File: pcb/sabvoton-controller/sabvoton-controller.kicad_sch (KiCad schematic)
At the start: 48 parts, among them J1 CONTROLLER_HALL, J2 CONN_MAIN, J3 ENGINE_HALL, J4 DISPLAY_CONNECTOR, Q1 BSS123, Q2 BSS123, Q3 BSS123, U1 ESP32-WROOM-32, U2 XL7015E1, U3 XL7015E1, U4 NCP1117-3.3_SOT223, U5 LM1117-1.8, U6 BTS4140N, U7 LM358

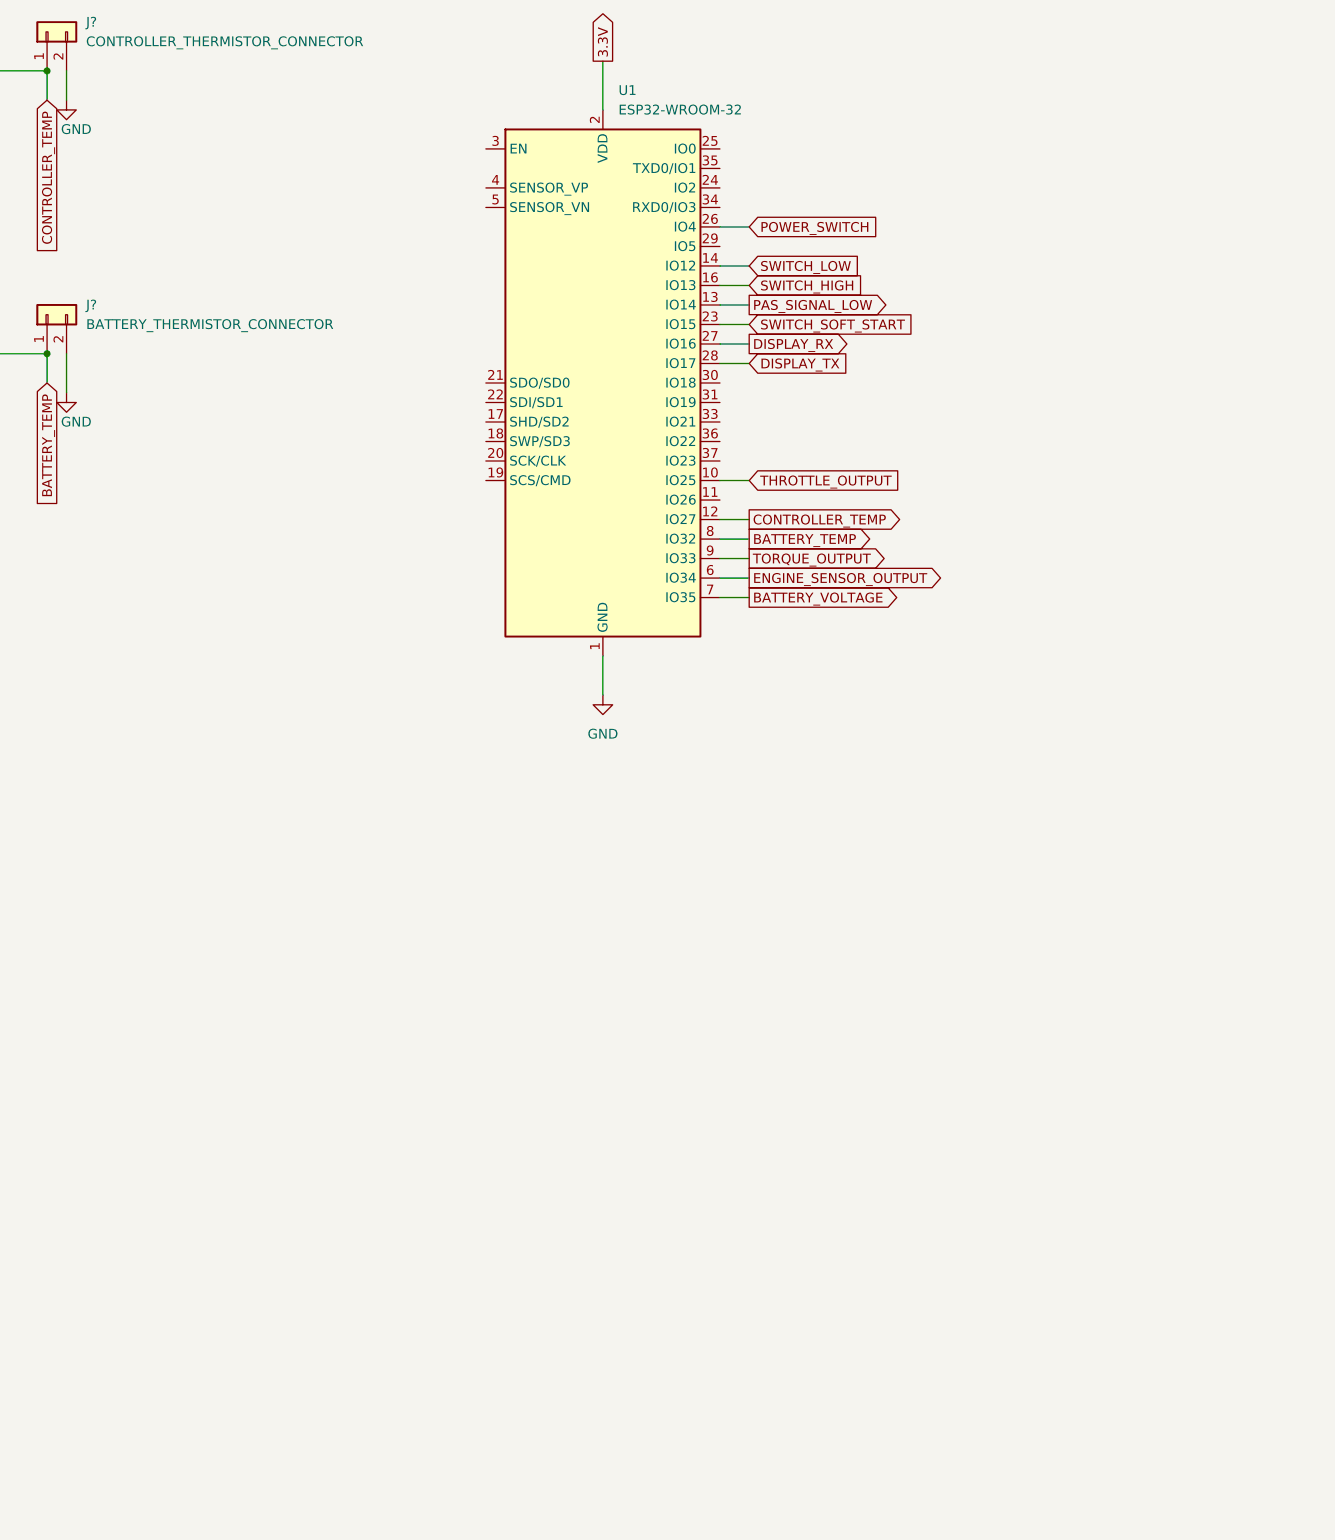
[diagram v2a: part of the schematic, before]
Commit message: Added USB connector
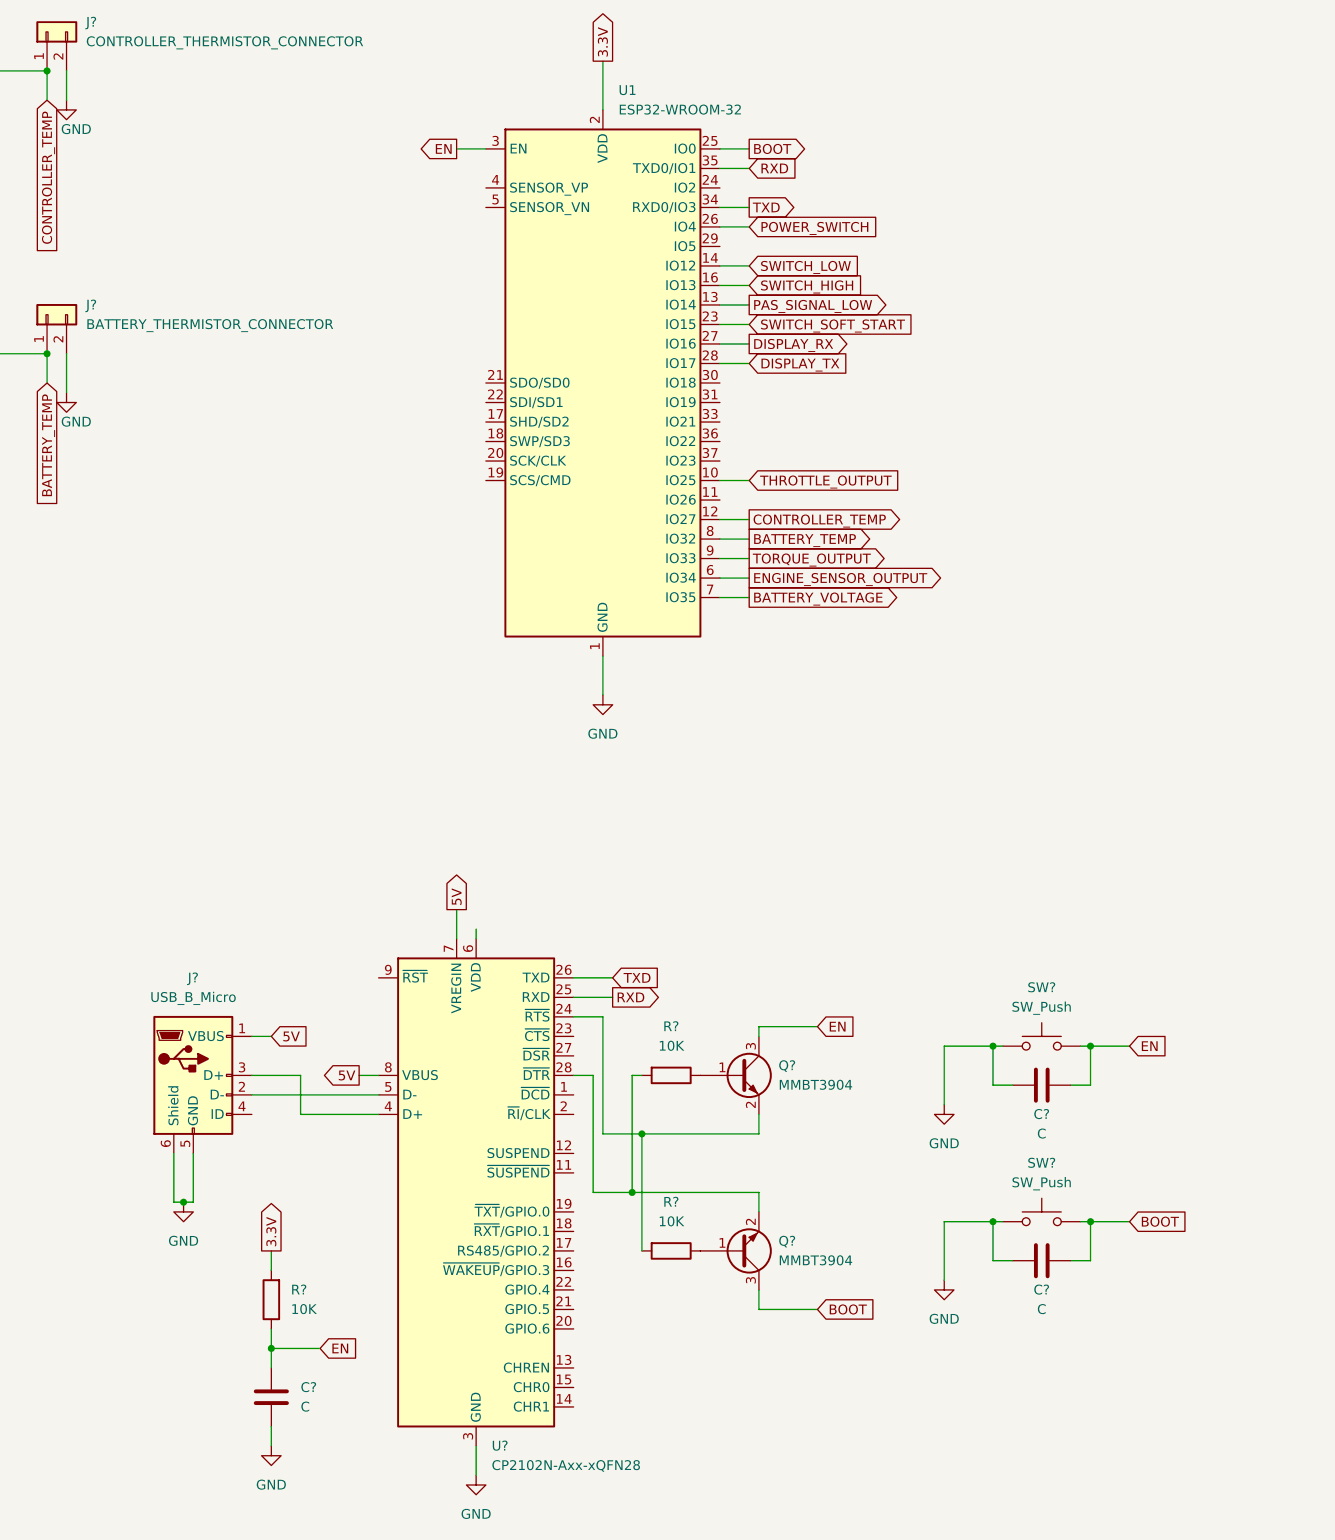
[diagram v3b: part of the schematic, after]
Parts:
- added C? (x3): C, symbol Device:C
- added J?: USB_B_Micro, symbol Connector:USB_B_Micro
- added Q? (x2): MMBT3904, Package_TO_SOT_SMD:SOT-23, symbol Transistor_BJT:MMBT3904
- added R? (x3): 10K, symbol Device:R
- added SW? (x2): SW_Push, symbol Switch:SW_Push
- added U?: CP2102N-Axx-xQFN28, Package_DFN_QFN:QFN-28-1EP_5x5mm_P0.5mm_EP3.35x3.35mm, symbol Interface_USB:CP2102N-Axx-xQFN28
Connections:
- net 3.3V: now also R?.2
- net 5V: now also J?.1 (VBUS), U?.7 (VREGIN), U?.8 (VBUS)
- net GND: now also C?.1, C?.1, C?.2, J?.5 (GND), J?.6 (Shield), SW?.1, SW?.1, U?.29 (GND), U?.3 (GND)
- net BOOT: now reaches U1.25 (IO0)
- net BOOT: now also C?.2, Q?.3 (C), SW?.2
- net EN: now reaches U1.3 (EN)
- net EN: now also C?.1, C?.2, Q?.3 (C), R?.1, SW?.2
- net TXD: now reaches U1.34 (RXD0/IO3)
- net TXD: now also U?.26 (TXD)
- net RXD: now reaches U1.35 (TXD0/IO1)
- net RXD: now also U?.25 (RXD)
- new net: Q?.1 (B), R?.1 (x2)
- new net: Q?.2 (E), R?.2, U?.24 (~{RTS})
- new net: J?.2 (D-), U?.5 (D-)
- new net: J?.3 (D+), U?.4 (D+)
- new net: Q?.2 (E), R?.2, U?.28 (~{DTR})

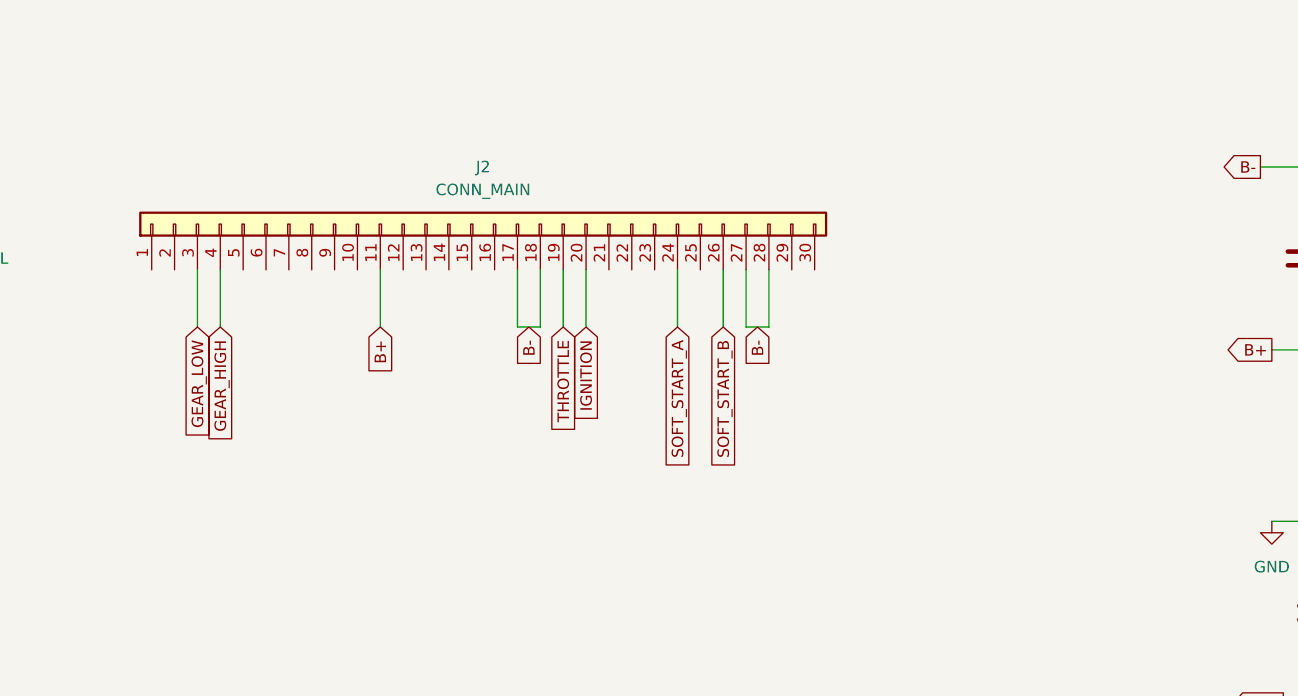
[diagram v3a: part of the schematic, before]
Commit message: Added programing connector
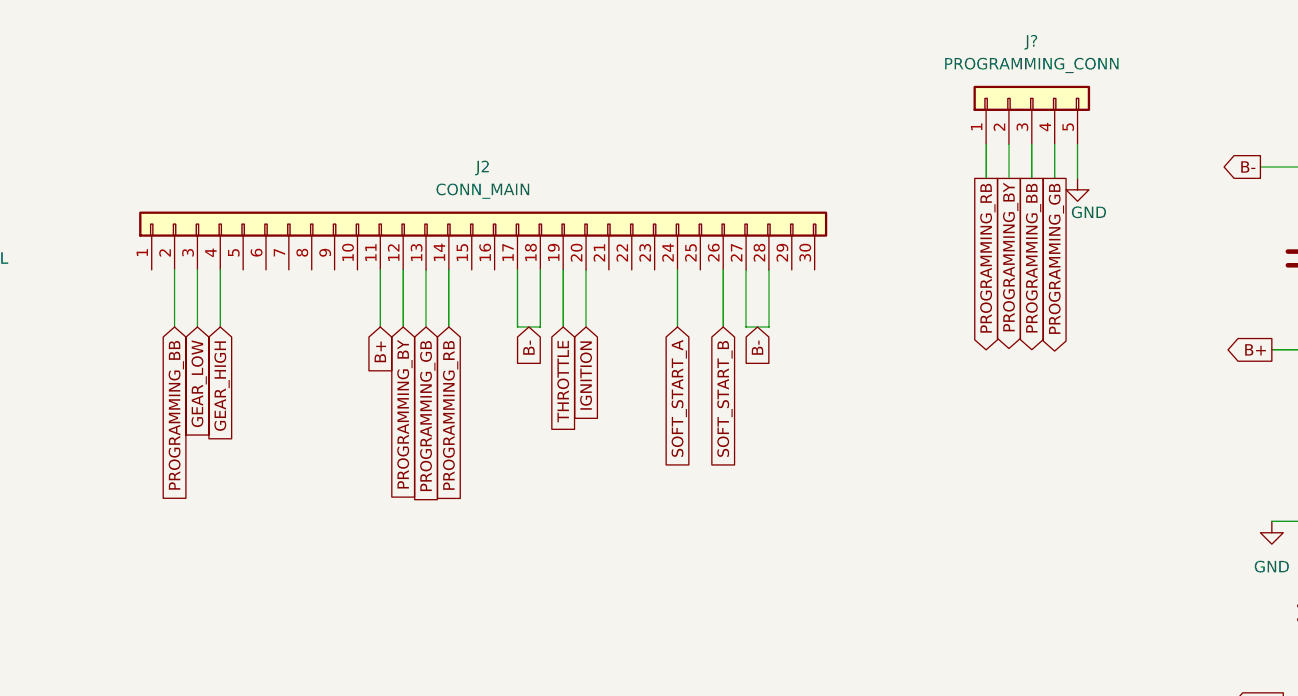
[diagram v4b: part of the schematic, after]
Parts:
- added J?: PROGRAMMING_CONN, symbol Connector_Generic:Conn_01x05
- J?: footprint (none) -> Connector_USB:USB_C_Plug_Molex_105444
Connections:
- net GND: now also J?.5 (Pin_5)
- net PROGRAMMING_BY: now reaches J2.12 (Pin_12)
- net PROGRAMMING_BY: now also J?.2 (Pin_2)
- net PROGRAMMING_GB: now reaches J2.13 (Pin_13)
- net PROGRAMMING_GB: now also J?.4 (Pin_4)
- net PROGRAMMING_RB: now reaches J2.14 (Pin_14)
- net PROGRAMMING_RB: now also J?.1 (Pin_1)
- net PROGRAMMING_BB: now reaches J2.2 (Pin_2)
- net PROGRAMMING_BB: now also J?.3 (Pin_3)
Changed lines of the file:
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@@
+    (stroke (width 0) (type default) (color 0 0 0 0))
+  )
+  (wire (pts (xy 472.44 45.72) (xy 472.44 49.53))
     (stroke (width 0) (type default) (color 0 0 0 0))
   )
@@
     (stroke (width 0) (type default) (color 0 0 0 0))
   )
+  (wire (pts (xy 467.36 45.72) (xy 467.36 49.53))
+    (stroke (width 0) (type default) (color 0 0 0 0))
+  )
   (wire (pts (xy 241.3 128.27) (xy 241.3 134.62))
     (stroke (width 0) (type default) (color 0 0 0 0))
   )
+  (wire (pts (xy 469.9 45.72) (xy 469.9 49.53))
+    (stroke (width 0) (type default) (color 0 0 0 0))
+  )
   (wire (pts (xy 519.43 147.32) (xy 521.97 147.32))
     (stroke (width 0) (type default) (color 0 0 0 0))
@@
     (stroke (width 0) (type default) (color 0 0 0 0))
   )
+  (wire (pts (xy 372.11 59.69) (xy 372.11 66.04))
+    (stroke (width 0) (type default) (color 0 0 0 0))
+  )
   (wire (pts (xy 398.78 267.97) (xy 398.78 265.43))
     (stroke (width 0) (type default) (color 0 0 0 0))
@@
     (stroke (width 0) (type default) (color 0 0 0 0))
   )
+  (wire (pts (xy 402.59 59.69) (xy 402.59 66.04))
+    (stroke (width 0) (type default) (color 0 0 0 0))
+  )
   (wire (pts (xy 332.74 252.73) (xy 349.25 252.73))
     (stroke (width 0) (type default) (color 0 0 0 0))
@@
     (stroke (width 0) (type default) (color 0 0 0 0))
   )
+  (wire (pts (xy 397.51 59.69) (xy 397.51 66.04))
+    (stroke (width 0) (type default) (color 0 0 0 0))
+  )
   (wire (pts (xy 251.46 120.65) (xy 251.46 123.19))
     (stroke (width 0) (type default) (color 0 0 0 0))
@@
     (stroke (width 0) (type default) (color 0 0 0 0))
   )
+  (wire (pts (xy 400.05 59.69) (xy 400.05 66.04))
+    (stroke (width 0) (type default) (color 0 0 0 0))
+  )
   (wire (pts (xy 231.14 107.95) (xy 234.95 107.95))
     (stroke (width 0) (type default) (color 0 0 0 0))
@@
     (stroke (width 0) (type default) (color 0 0 0 0))
   )
+  (wire (pts (xy 462.28 45.72) (xy 462.28 49.53))
+    (stroke (width 0) (type default) (color 0 0 0 0))
+  )
   (wire (pts (xy 513.08 180.34) (xy 516.89 180.34))
     (stroke (width 0) (type default) (color 0 0 0 0))
@@
     (stroke (width 0) (type default) (color 0 0 0 0))
   )
+  (wire (pts (xy 464.82 45.72) (xy 464.82 49.53))
+    (stroke (width 0) (type default) (color 0 0 0 0))
+  )
   (wire (pts (xy 499.11 101.6) (xy 499.11 107.95))
     (stroke (width 0) (type default) (color 0 0 0 0))
@@
     )
   )
+  (global_label "PROGRAMMING_GB" (shape output) (at 469.9 49.53 270) (fields_autoplaced)
+    (effects (font (size 1.27 1.27)) (justify right))
+    (property "Intersheet References" "${INTERSHEET_REFS}" (id 0) (at 469.8206 69.0579 90)
+      (effects (font (size 1.27 1.27)) (justify right) hide)
+    )
+  )
   (global_label "TXD" (shape output) (at 397.51 137.16 0) (fields_autoplaced)
     (effects (font (size 1.27 1.27)) (justify left))
@@
     )
   )
+  (global_label "PROGRAMMING_BY" (shape output) (at 464.82 49.53 270) (fields_autoplaced)
+    (effects (font (size 1.27 1.27)) (justify right))
+    (property "Intersheet References" "${INTERSHEET_REFS}" (id 0) (at 464.7406 68.8764 90)
+      (effects (font (size 1.27 1.27)) (justify right) hide)
+    )
+  )
   (global_label "SWITCH_HIGH" (shape input) (at 397.51 147.32 0) (fields_autoplaced)
     (effects (font (size 1.27 1.27)) (justify left))
@@
     )
   )
+  (global_label "PROGRAMMING_RB" (shape input) (at 402.59 66.04 270) (fields_autoplaced)
+    (effects (font (size 1.27 1.27)) (justify right))
+    (property "Intersheet References" "${INTERSHEET_REFS}" (id 0) (at 402.5106 85.5679 90)
+      (effects (font (size 1.27 1.27)) (justify right) hide)
+    )
+  )
   (global_label "POWER_SWITCH" (shape input) (at 397.51 139.7 0) (fields_autoplaced)
     (effects (font (size 1.27 1.27)) (justify left))
@@
     )
   )
+  (global_label "PROGRAMMING_BB" (shape input) (at 372.11 66.04 270) (fields_autoplaced)
+    (effects (font (size 1.27 1.27)) (justify right))
+    (property "Intersheet References" "${INTERSHEET_REFS}" (id 0) (at 372.0306 85.5679 90)
+      (effects (font (size 1.27 1.27)) (justify right) hide)
+    )
+  )
   (global_label "BATTERY_TEMP" (shape input) (at 306.07 160.02 270) (fields_autoplaced)
     (effects (font (size 1.27 1.27)) (justify right))
@@
     )
   )
+  (global_label "PROGRAMMING_BB" (shape output) (at 467.36 49.53 270) (fields_autoplaced)
+    (effects (font (size 1.27 1.27)) (justify right))
+    (property "Intersheet References" "${INTERSHEET_REFS}" (id 0) (at 467.2806 69.0579 90)
+      (effects (font (size 1.27 1.27)) (justify right) hide)
+    )
+  )
   (global_label "B+" (shape input) (at 394.97 66.04 270) (fields_autoplaced)
     (effects (font (size 1.27 1.27)) (justify right))
@@
     )
   )
+  (global_label "PROGRAMMING_RB" (shape output) (at 462.28 49.53 270) (fields_autoplaced)
+    (effects (font (size 1.27 1.27)) (justify right))
+    (property "Intersheet References" "${INTERSHEET_REFS}" (id 0) (at 462.2006 69.0579 90)
+      (effects (font (size 1.27 1.27)) (justify right) hide)
+    )
+  )
   (global_label "THROTTLE" (shape input) (at 196.85 130.81 0) (fields_autoplaced)
     (effects (font (size 1.27 1.27)) (justify left))
@@
     )
   )
+  (global_label "PROGRAMMING_GB" (shape input) (at 400.05 66.04 270) (fields_autoplaced)
+    (effects (font (size 1.27 1.27)) (justify right))
+    (property "Intersheet References" "${INTERSHEET_REFS}" (id 0) (at 399.9706 85.5679 90)
+      (effects (font (size 1.27 1.27)) (justify right) hide)
+    )
+  )
   (global_label "SOFT_START_B" (shape output) (at 213.36 219.71 0) (fields_autoplaced)
     (effects (font (size 1.27 1.27)) (justify left))
     (property "Intersheet References" "${INTERSHEET_REFS}" (id 0) (at 229.0779 219.6306 0)
       (effects (font (size 1.27 1.27)) (justify left) hide)
+    )
+  )
+  (global_label "PROGRAMMING_BY" (shape input) (at 397.51 66.04 270) (fields_autoplaced)
+    (effects (font (size 1.27 1.27)) (justify right))
+    (property "Intersheet References" "${INTERSHEET_REFS}" (id 0) (at 397.4306 85.3864 90)
+      (effects (font (size 1.27 1.27)) (justify right) hide)
     )
   )
@@
     (pin "2")
   )
+  (symbol (lib_id "Connector_Generic:Conn_01x05") (at 467.36 40.64 90) (unit 1)
+    (in_bom yes) (on_board yes) (fields_autoplaced)
+    (property "Reference" "J?" (id 0) (at 467.36 34.29 90))
+    (property "Value" "PROGRAMMING_CONN" (id 1) (at 467.36 36.83 90))
+    (property "Footprint" "" (id 2) (at 467.36 40.64 0)
+      (effects (font (size 1.27 1.27)) hide)
+    )
+    (property "Datasheet" "~" (id 3) (at 467.36 40.64 0)
+      (effects (font (size 1.27 1.27)) hide)
+    )
+    (pin "1")
+    (pin "2")
+    (pin "3")
+    (pin "4")
+    (pin "5")
+  )
   (symbol (lib_id "Transistor_BJT:MMBT3904") (at 396.24 250.19 0) (unit 1)
     (in_bom yes) (on_board yes) (fields_autoplaced)
@@
     (property "Reference" "J?" (id 0) (at 325.12 237.49 0))
     (property "Value" "USB_B_Micro" (id 1) (at 325.12 240.03 0))
-    (property "Footprint" "" (id 2) (at 328.93 251.46 0)
+    (property "Footprint" "Connector_USB:USB_C_Plug_Molex_105444" (id 2) (at 328.93 251.46 0)
       (effects (font (size 1.27 1.27)) hide)
     )
@@
     (pin "2")
     (pin "3")
+  )
+  (symbol (lib_id "power:GND") (at 472.44 49.53 0) (unit 1)
+    (in_bom yes) (on_board yes)
+    (property "Reference" "#PWR?" (id 0) (at 472.44 55.88 0)
+      (effects (font (size 1.27 1.27)) hide)
+    )
+    (property "Value" "GND" (id 1) (at 473.71 53.34 0))
+    (property "Footprint" "" (id 2) (at 472.44 49.53 0)
+      (effects (font (size 1.27 1.27)) hide)
+    )
+    (property "Datasheet" "" (id 3) (at 472.44 49.53 0)
+      (effects (font (size 1.27 1.27)) hide)
+    )
+    (pin "1")
   )
   (symbol (lib_id "Device:C") (at 548.64 64.77 0) (unit 1)
@@
       (reference "#PWR?") (unit 1) (value "GND") (footprint "")
     )
+    (path "/bee02de4-2867-4c42-bc59-fa68ac2e4c58"
+      (reference "#PWR?") (unit 1) (value "GND") (footprint "")
+    )
     (path "/bffbea91-1453-4222-9684-3547fdd9e180"
       (reference "#PWR?") (unit 1) (value "GND") (footprint "")
@@
       (reference "J4") (unit 1) (value "DISPLAY_CONNECTOR") (footprint "")
     )
+    (path "/36c3c38d-a416-41d4-a414-731a707799a3"
+      (reference "J?") (unit 1) (value "PROGRAMMING_CONN") (footprint "")
+    )
     (path "/607b52a9-80ae-4728-a091-19987d7df497"
